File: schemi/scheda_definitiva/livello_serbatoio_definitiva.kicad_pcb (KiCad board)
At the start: 2 copper layers, 83 x 72 mm, 45 parts, among them J1 USB_B, J2 BTN_LED_GROUP, J3 CONN_LCD, J4 CONN_US, J5 ICSP, J7 Exp_Analog, SW1 SW_RST, U1 FT232RL, U2 ATmega328P-PU, U3 USBLC6-2SC6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

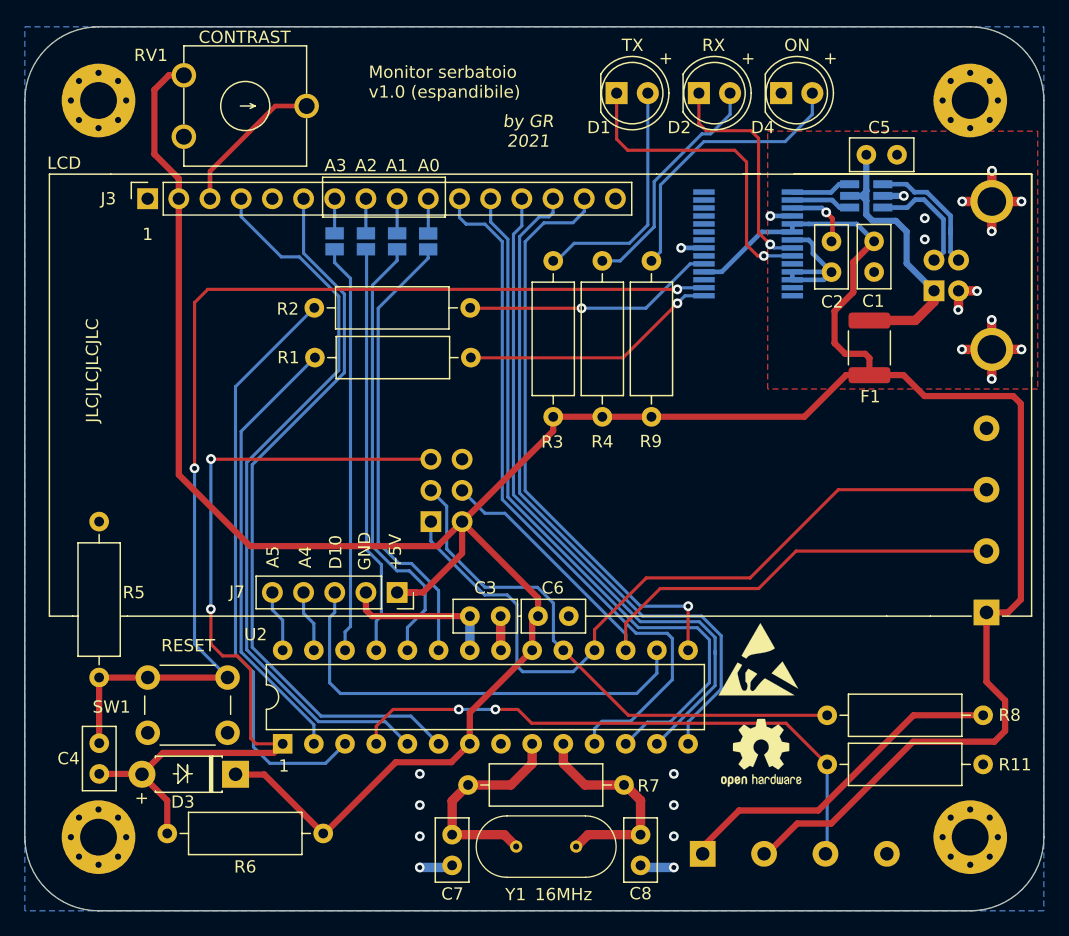
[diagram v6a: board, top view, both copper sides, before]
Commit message: revisionata connessione DTR logica reset - revisionato wiring DTR - aggiornato PCB - ricreato gerber
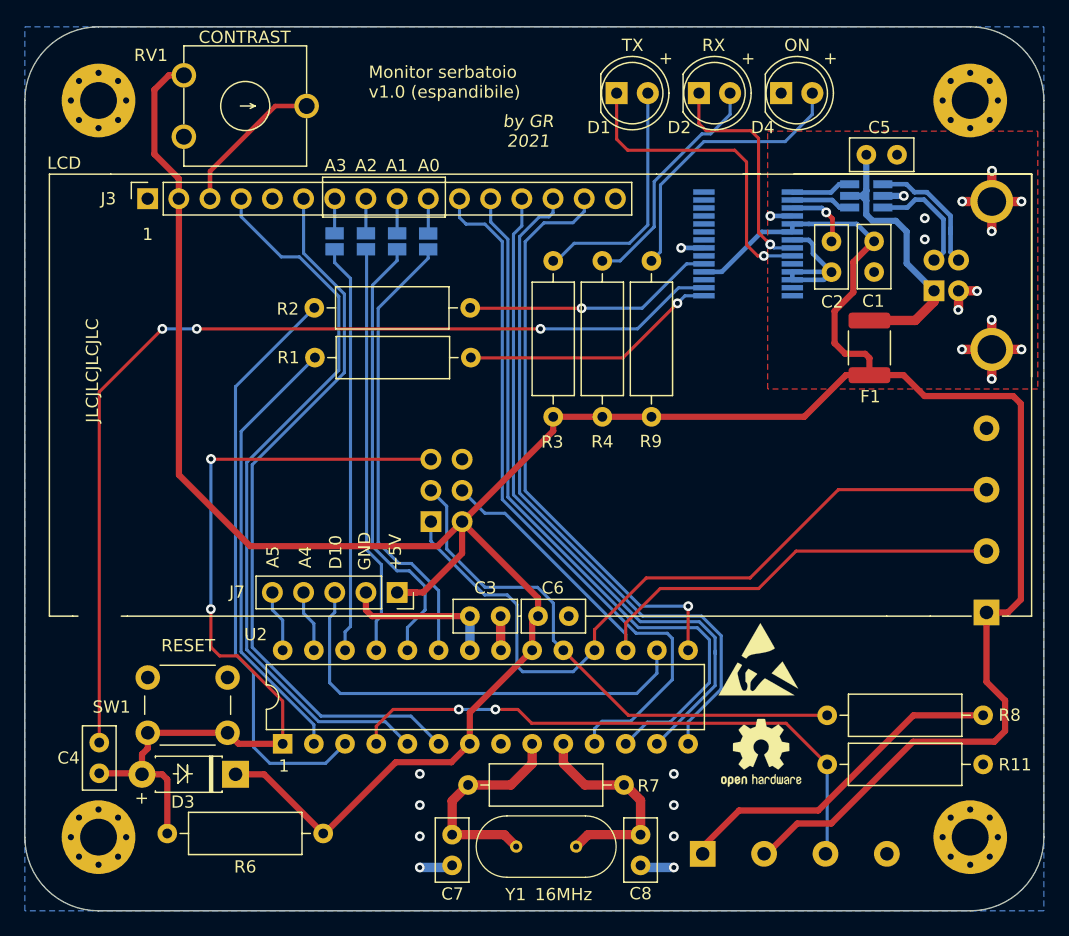
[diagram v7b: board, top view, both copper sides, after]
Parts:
- removed R5: 1k, Resistor_THT:R_Axial_DIN0309_L9.0mm_D3.2mm_P12.70mm_Horizontal
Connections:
- SW1 pad 1: DTR -> GND
- SW1 pad 2: GND -> ICSP_RST
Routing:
- net DTR: track 89.6 -> 81.3 mm, vias 2 -> 3
- net ICSP_RST: track 67.4 -> 70.1 mm

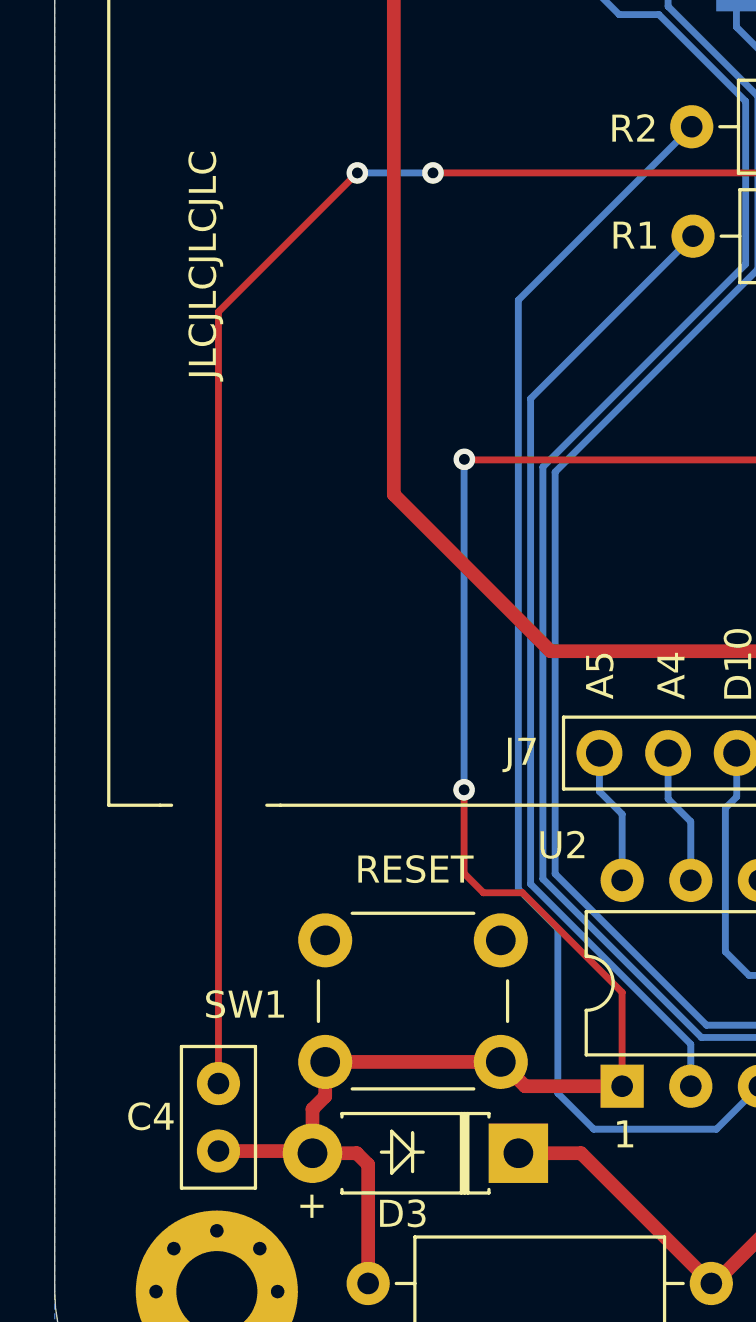
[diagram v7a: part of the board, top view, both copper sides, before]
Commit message: revisione piste circuito reset - spostata pista DTR - spostato pulsante - aggiornato piano di massa - rimossa una via su DTR
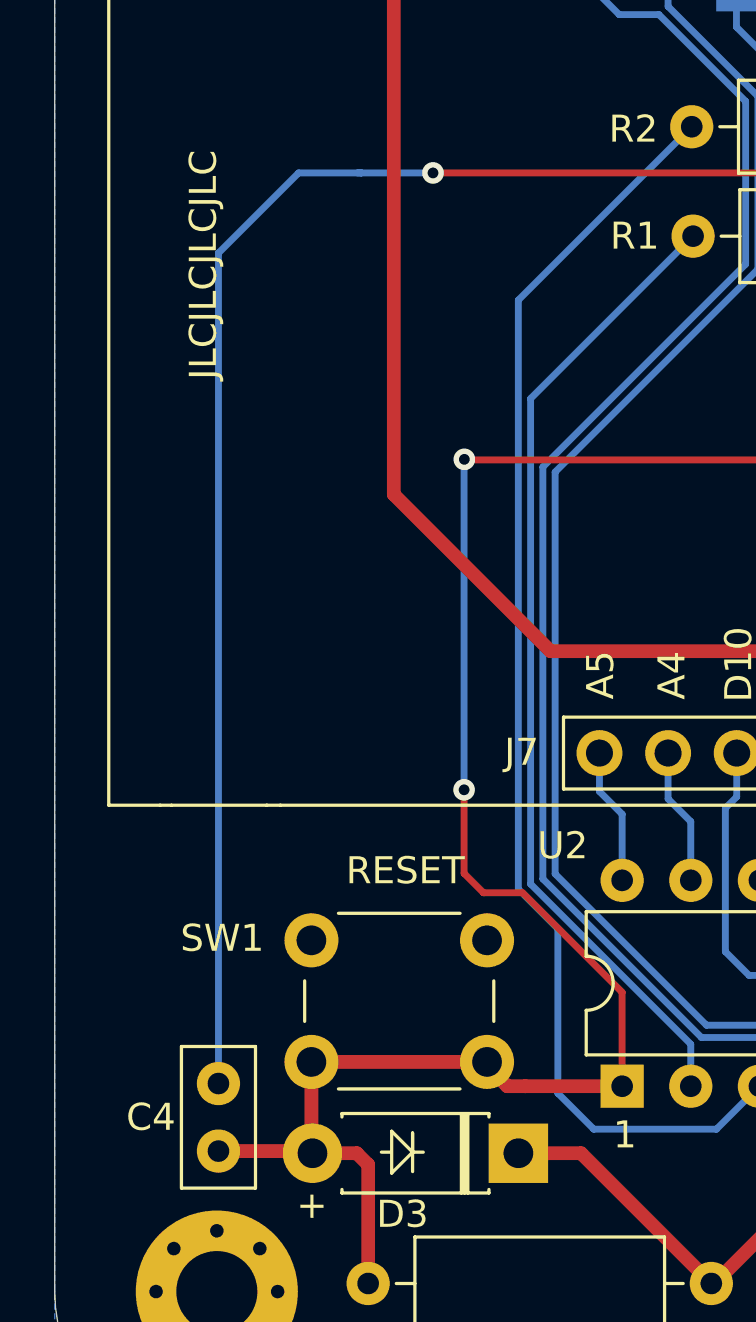
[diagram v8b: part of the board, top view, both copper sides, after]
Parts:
- moved SW1 0.51 mm to (96.5, 121.0)
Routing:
- net DTR: track 81.3 -> 82.7 mm, vias 3 -> 2
